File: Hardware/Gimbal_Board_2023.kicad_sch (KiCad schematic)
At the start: 77 parts, among them J1 6P6C, J2 RJ45_LED_Shielded, Q1 Q_NMOS_GDS, Q2 Q_NMOS_GDS, Q3 Q_NMOS_GDS, Q4 Q_NMOS_GDS, Q5 Q_NMOS_GDS, Q6 Q_NMOS_GDS, Q7 Q_NMOS_GDS, Q8 Q_NMOS_GDS, SW1 SW_Push, SW2 SW_Push, SW3 SW_Push, SW4 SW_Push, SW5 SW_Push, SW6 SW_Push, SW7 SW_Push, SW8 SW_Push, SW9 SW_DPDT_x2, U3 Teensy4.1_DEV-16771, U3.3 TSR_1-2450, U5 TSR_1-2450

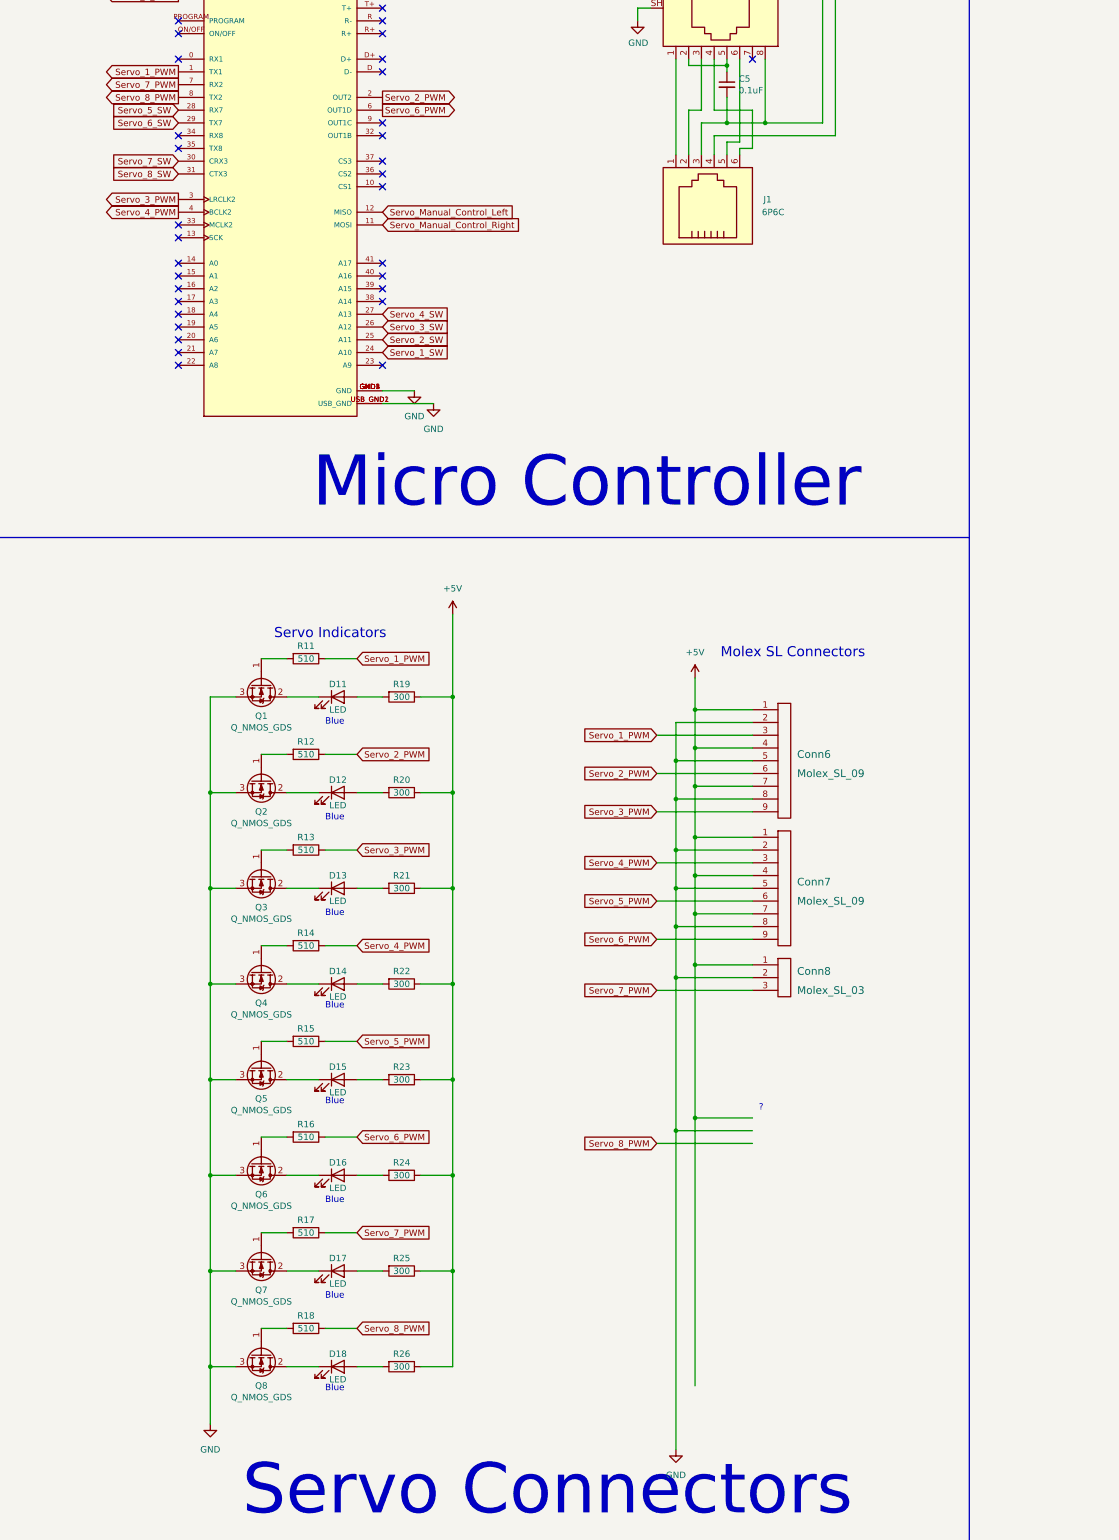
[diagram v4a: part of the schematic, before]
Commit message: Merged Grounds Changed Leds
Merged Grounds on the Teensy
Changed Servo control LEDs to yellow
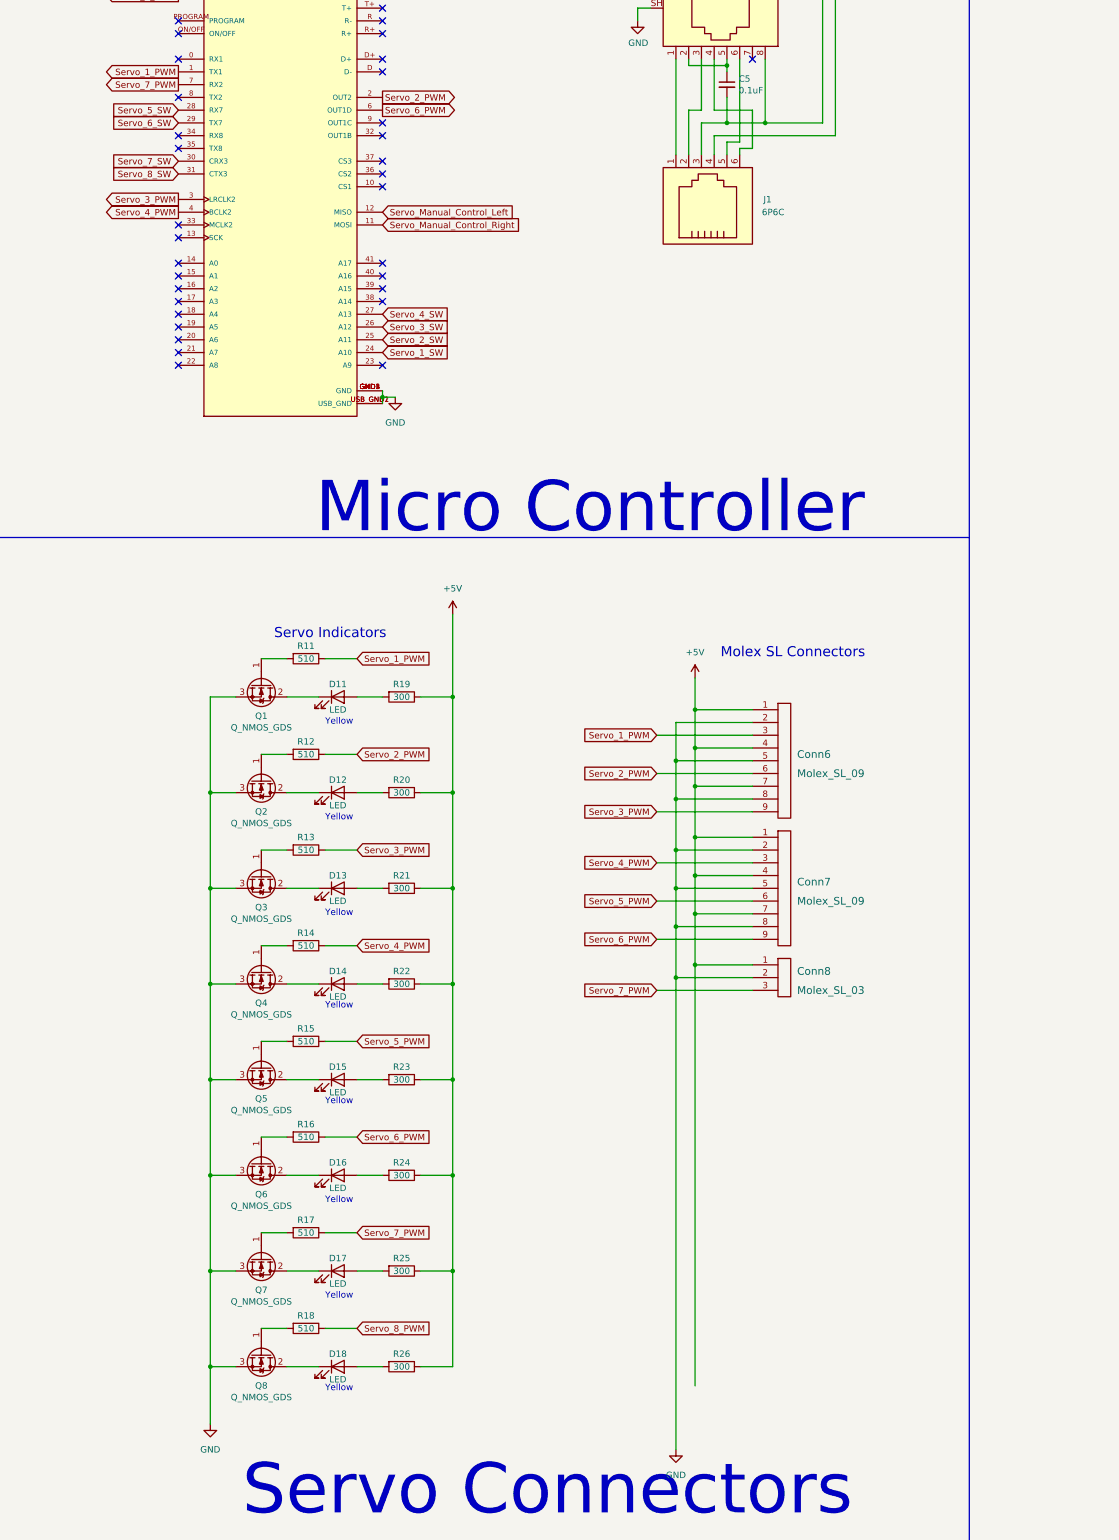
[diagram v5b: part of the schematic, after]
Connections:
- net Servo_8_PWM: no longer U3.8 (TX2)
- no-connect marks 40 -> 41
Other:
- note added: "Yellow"
- note removed: "?"
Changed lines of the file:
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@@
   (junction (at 81.28 229.87) (diameter 0) (color 0 0 0 0)
   )
-  (junction (at 416.56 262.89) (diameter 0) (color 0 0 0 0)
-  )
   (junction (at 416.56 222.25) (diameter 0) (color 0 0 0 0)
   )
@@
   (junction (at 368.3 179.07) (diameter 0) (color 0 0 0 0)
   )
-  (junction (at 412.75 265.43) (diameter 0) (color 0 0 0 0)
-  )
   (junction (at 81.28 295.91) (diameter 0) (color 0 0 0 0)
   )
@@
   )
   (junction (at 368.3 236.22) (diameter 0) (color 0 0 0 0)
+  )
+  (junction (at 354.33 119.38) (diameter 0) (color 0 0 0 0)
   )
   (junction (at 412.75 217.17) (diameter 0) (color 0 0 0 0)
@@
   (no_connect (at 415.29 31.75))
   (no_connect (at 313.69 52.07))
+  (no_connect (at 313.69 59.69))
   (no_connect (at 354.33 113.03))
   (no_connect (at 354.33 64.77))
@@
     (stroke (width 0) (type default) (color 0 0 0 0))
   )
+  (wire (pts (xy 354.33 118.11) (xy 354.33 119.38))
+    (stroke (width 0) (type default) (color 0 0 0 0))
+  )
   (wire (pts (xy 45.72 196.85) (xy 49.53 196.85))
     (stroke (width 0) (type default) (color 0 0 0 0))
@@
     (stroke (width 0) (type default) (color 0 0 0 0))
   )
-  (wire (pts (xy 427.99 265.43) (xy 412.75 265.43))
-    (stroke (width 0) (type default) (color 0 0 0 0))
-  )
   (wire (pts (xy 166.37 173.99) (xy 165.1 173.99))
     (stroke (width 0) (type default) (color 0 0 0 0))
@@
     (stroke (width 0) (type default) (color 0 0 0 0))
   )
+  (wire (pts (xy 354.33 119.38) (xy 356.87 119.38))
+    (stroke (width 0) (type default) (color 0 0 0 0))
+  )
   (wire (pts (xy 45.72 295.91) (xy 49.53 295.91))
     (stroke (width 0) (type default) (color 0 0 0 0))
@@
     (stroke (width 0) (type default) (color 0 0 0 0))
   )
-  (wire (pts (xy 354.33 118.11) (xy 360.68 118.11))
-    (stroke (width 0) (type default) (color 0 0 0 0))
-  )
   (wire (pts (xy 173.99 204.47) (xy 184.15 204.47))
     (stroke (width 0) (type default) (color 0 0 0 0))
@@
     (stroke (width 0) (type default) (color 0 0 0 0))
   )
-  (wire (pts (xy 412.75 265.43) (xy 412.75 328.93))
-    (stroke (width 0) (type default) (color 0 0 0 0))
-  )
   (wire (pts (xy 325.12 312.42) (xy 320.04 312.42))
     (stroke (width 0) (type default) (color 0 0 0 0))
@@
     (stroke (width 0) (type default) (color 0 0 0 0))
   )
-  (wire (pts (xy 416.56 232.41) (xy 416.56 262.89))
-    (stroke (width 0) (type default) (color 0 0 0 0))
-  )
   (wire (pts (xy 330.2 171.45) (xy 335.28 171.45))
     (stroke (width 0) (type default) (color 0 0 0 0))
@@
     (stroke (width 0) (type default) (color 0 0 0 0))
   )
-  (wire (pts (xy 416.56 262.89) (xy 416.56 316.23))
-    (stroke (width 0) (type default) (color 0 0 0 0))
-  )
-  (wire (pts (xy 412.75 234.95) (xy 412.75 265.43))
+  (wire (pts (xy 416.56 232.41) (xy 416.56 316.23))
+    (stroke (width 0) (type default) (color 0 0 0 0))
+  )
+  (wire (pts (xy 412.75 234.95) (xy 412.75 328.93))
     (stroke (width 0) (type default) (color 0 0 0 0))
   )
@@
     (stroke (width 0) (type default) (color 0 0 0 0))
   )
+  (wire (pts (xy 354.33 119.38) (xy 354.33 120.65))
+    (stroke (width 0) (type default) (color 0 0 0 0))
+  )
   (polyline (pts (xy 471.17 0) (xy 471.17 147.32))
     (stroke (width 0) (type default) (color 0 0 0 0))
@@
     (stroke (width 0) (type default) (color 0 0 0 0))
   )
-  (wire (pts (xy 427.99 262.89) (xy 416.56 262.89))
-    (stroke (width 0) (type default) (color 0 0 0 0))
-  )
   (wire (pts (xy 172.72 179.07) (xy 172.72 185.42))
     (stroke (width 0) (type default) (color 0 0 0 0))
@@
     (stroke (width 0) (type default) (color 0 0 0 0))
   )
-  (wire (pts (xy 354.33 120.65) (xy 364.49 120.65))
-    (stroke (width 0) (type default) (color 0 0 0 0))
-  )
   (polyline (pts (xy 271.78 147.32) (xy 245.11 147.32))
     (stroke (width 0) (type default) (color 0 0 0 0))
@@
     (stroke (width 0) (type default) (color 0 0 0 0))
   )
-  (wire (pts (xy 427.99 267.97) (xy 408.94 267.97))
-    (stroke (width 0) (type default) (color 0 0 0 0))
-  )
   (wire (pts (xy 27.94 179.07) (xy 27.94 170.18))
     (stroke (width 0) (type default) (color 0 0 0 0))
@@
     (stroke (width 0) (type default) (color 0 0 0 0))
   )
-  (text "?\n" (at 429.26 261.62 0)
-    (effects (font (size 1.27 1.27)) (justify left bottom))
-  )
-  (text "Blue" (at 342.9 241.3 0)
+  (text "Yellow" (at 342.9 241.3 0)
     (effects (font (size 1.27 1.27)) (justify left bottom))
   )
@@
     (effects (font (size 1.27 1.27)) (justify left bottom))
   )
-  (text "Blue" (at 342.9 317.5 0)
+  (text "Yellow" (at 342.9 317.5 0)
     (effects (font (size 1.27 1.27)) (justify left bottom))
   )
@@
     (effects (font (size 1.27 1.27)) (justify left bottom))
   )
-  (text "Blue" (at 342.9 222.885 0)
+  (text "Yellow" (at 342.9 222.885 0)
     (effects (font (size 1.27 1.27)) (justify left bottom))
   )
@@
     (effects (font (size 1.27 1.27)) (justify left bottom))
   )
-  (text "Micro Controller" (at 340.36 142.24 0)
+  (text "Micro Controller" (at 340.995 147.32 0)
     (effects (font (size 10 10)) (justify left bottom))
   )
@@
     (effects (font (size 1.27 1.27)) (justify left bottom))
   )
-  (text "Blue" (at 342.9 280.035 0)
+  (text "Yellow" (at 342.9 280.035 0)
     (effects (font (size 1.27 1.27)) (justify left bottom))
   )
@@
     (effects (font (size 2.0066 2.0066)) (justify left bottom))
   )
-  (text "Blue" (at 342.9 299.085 0)
+  (text "Yellow" (at 342.9 299.085 0)
     (effects (font (size 1.27 1.27)) (justify left bottom))
   )
@@
     (effects (font (size 10 10)) (justify left bottom))
   )
-  (text "Blue" (at 342.9 203.835 0)
+  (text "Yellow" (at 342.9 203.835 0)
     (effects (font (size 1.27 1.27)) (justify left bottom))
   )
-  (text "Blue" (at 342.9 260.35 0)
+  (text "Yellow" (at 342.9 260.35 0)
     (effects (font (size 1.27 1.27)) (justify left bottom))
   )
-  (text "Blue" (at 342.9 184.785 0)
+  (text "Yellow" (at 342.9 184.785 0)
     (effects (font (size 1.27 1.27)) (justify left bottom))
   )
@@
     )
   )
-  (global_label "Servo_8_PWM" (shape output) (at 313.69 59.69 180) (fields_autoplaced)
-    (effects (font (size 1.27 1.27)) (justify right))
-    (property "Intersheet References" "${INTERSHEET_REFS}" (id 0) (at 298.7583 59.6106 0)
-      (effects (font (size 1.27 1.27)) (justify right) hide)
-    )
-  )
   (global_label "Servo_7_PWM" (shape input) (at 349.25 285.75 0) (fields_autoplaced)
     (effects (font (size 1.27 1.27)) (justify left))
@@
     (property "Intersheet References" "${INTERSHEET_REFS}" (id 0) (at 68.0298 203.1206 0)
       (effects (font (size 1.27 1.27)) (justify left) hide)
-    )
-  )
-  (global_label "Servo_8_PWM" (shape input) (at 408.94 267.97 180) (fields_autoplaced)
-    (effects (font (size 1.27 1.27)) (justify right))
-    (property "Intersheet References" "${INTERSHEET_REFS}" (id 0) (at 394.0083 267.8906 0)
-      (effects (font (size 1.27 1.27)) (justify right) hide)
     )
   )
@@
     (pin "2")
   )
-  (symbol (lib_id "power:GND") (at 360.68 118.11 0) (unit 1)
-    (in_bom yes) (on_board yes) (fields_autoplaced)
-    (property "Reference" "#PWR06" (id 0) (at 360.68 124.46 0)
-      (effects (font (size 1.27 1.27)) hide)
-    )
-    (property "Value" "GND" (id 1) (at 360.68 123.19 0))
-    (property "Footprint" "" (id 2) (at 360.68 118.11 0)
-      (effects (font (size 1.27 1.27)) hide)
-    )
-    (property "Datasheet" "" (id 3) (at 360.68 118.11 0)
-      (effects (font (size 1.27 1.27)) hide)
-    )
-    (pin "1")
-  )
   (symbol (lib_id "Device:Q_NMOS_GDS") (at 330.2 214.63 270) (unit 1)
     (in_bom yes) (on_board yes)
@@
     (pin "2")
   )
-  (symbol (lib_id "power:GND") (at 364.49 120.65 0) (unit 1)
+  (symbol (lib_id "power:GND") (at 356.87 119.38 0) (unit 1)
     (in_bom yes) (on_board yes) (fields_autoplaced)
-    (property "Reference" "#PWR08" (id 0) (at 364.49 127 0)
-      (effects (font (size 1.27 1.27)) hide)
-    )
-    (property "Value" "GND" (id 1) (at 364.49 125.73 0))
-    (property "Footprint" "" (id 2) (at 364.49 120.65 0)
-      (effects (font (size 1.27 1.27)) hide)
-    )
-    (property "Datasheet" "" (id 3) (at 364.49 120.65 0)
+    (property "Reference" "#PWR08" (id 0) (at 356.87 125.73 0)
+      (effects (font (size 1.27 1.27)) hide)
+    )
+    (property "Value" "GND" (id 1) (at 356.87 124.46 0))
+    (property "Footprint" "" (id 2) (at 356.87 119.38 0)
+      (effects (font (size 1.27 1.27)) hide)
+    )
+    (property "Datasheet" "" (id 3) (at 356.87 119.38 0)
       (effects (font (size 1.27 1.27)) hide)
     )
@@
       (reference "#PWR05") (unit 1) (value "GND") (footprint "")
     )
-    (path "/25f41cd1-063c-4573-a753-45d1952a6bf4"
-      (reference "#PWR06") (unit 1) (value "GND") (footprint "")
-    )
     (path "/56650ab2-c12b-4ed7-8569-e8819d54634a"

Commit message: Checking save
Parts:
- renumbered D20 to DG0, D21 to DG1, D19 to DG2, D9 to DY01, D10 to DY02, D11 to DY1, D12 to DY2, D13 to DY3, D14 to DY4, D15 to DY5, D16 to DY6, D17 to DY7, D18 to DY8
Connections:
- net GND: now also U3. (USB_GND), U3.GND1-5 (GND), U3.USB_GND1-2 (USB_GND); no longer U3.GND1 (GND), U3.GND2 (GND), U3.GND3 (GND), U3.GND4 (GND), U3.GND5 (GND), U3.USB_GND1 (USB_GND), U3.USB_GND2 (USB_GND)
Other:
- moved on the sheet: Conn6, Conn7, Conn8

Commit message: Rearranged and cleaned up
Cleaned up Loose ends on circuits
Rearranged some
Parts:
- removed D8, DY8: LED, LED_SMD:LED_0603_1608Metric_Pad1.05x0.95mm_HandSolder, symbol Device:LED
- removed Q8: Q_NMOS_GDS, Package_TO_SOT_SMD:SOT-23, symbol Device:Q_NMOS_GDS
- removed R18: 510, Resistor_SMD:R_0603_1608Metric_Pad0.98x0.95mm_HandSolder, symbol Device:R
- removed R26: 300, Resistor_SMD:R_0603_1608Metric_Pad0.98x0.95mm_HandSolder, symbol Device:R
- removed R8: 100, Resistor_SMD:R_0603_1608Metric_Pad0.98x0.95mm_HandSolder, symbol Device:R
- removed SW8: SW_Push, Button_Switch_SMD:SW_SPST_EVPBF, symbol Switch:SW_Push
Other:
- moved on the sheet: C5, Conn1A, Conn1D, Conn6, Conn7, Conn8, D1, D2, D3, D4, D5, D6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
